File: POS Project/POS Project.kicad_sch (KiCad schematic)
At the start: 15 parts, among them J1 JST_2mm_LiPo, P1 USB_C_Plug_USB2.0, U1 MCP73831-2-OT

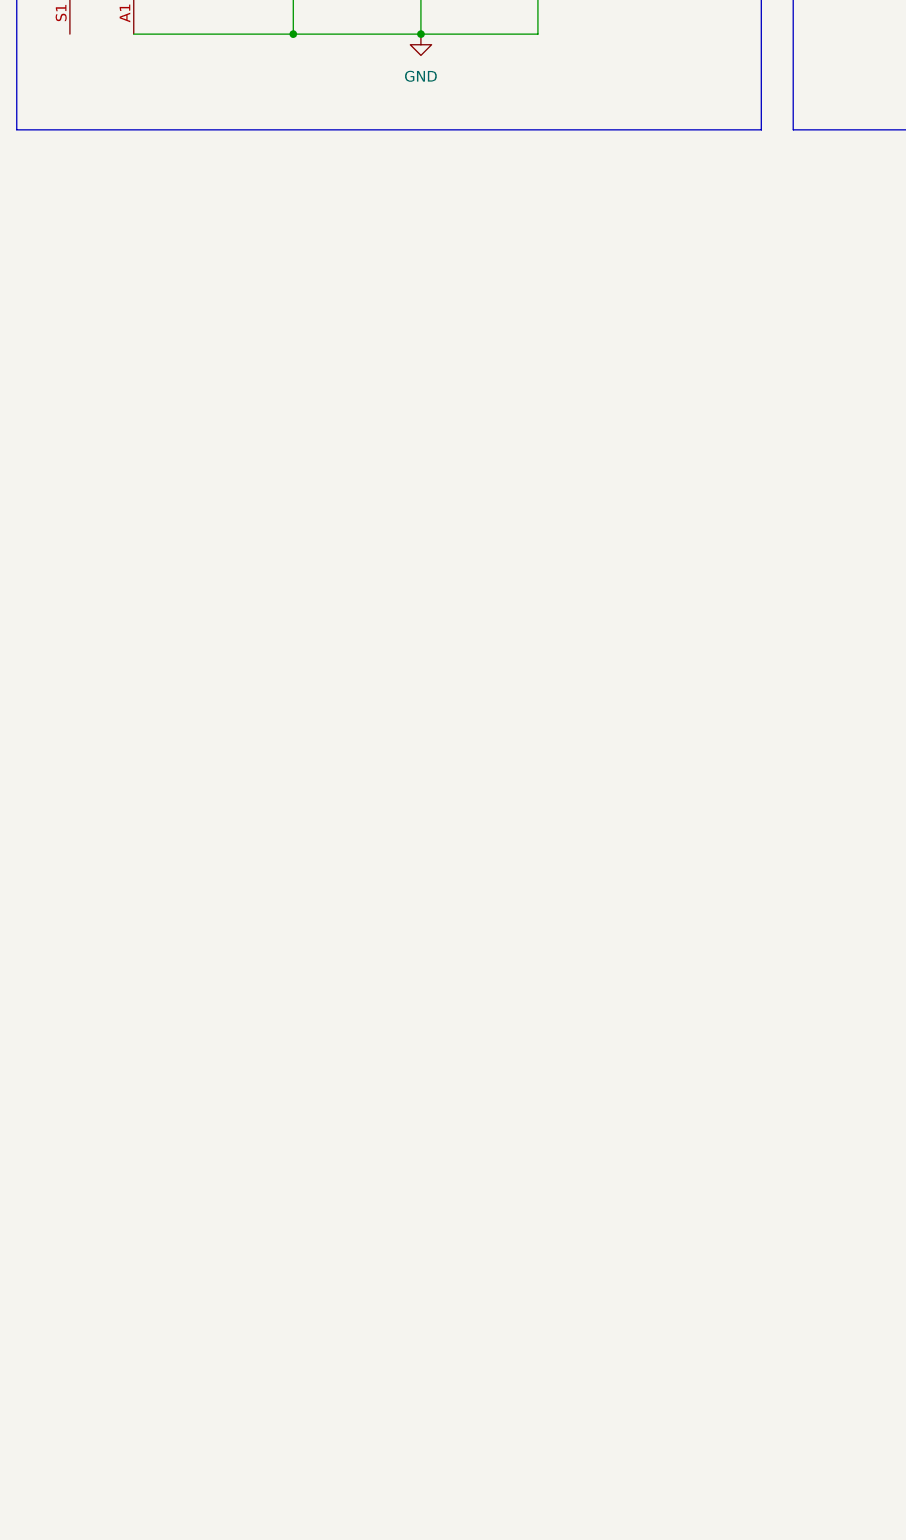
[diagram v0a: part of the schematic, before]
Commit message: modified sim7600x symbol
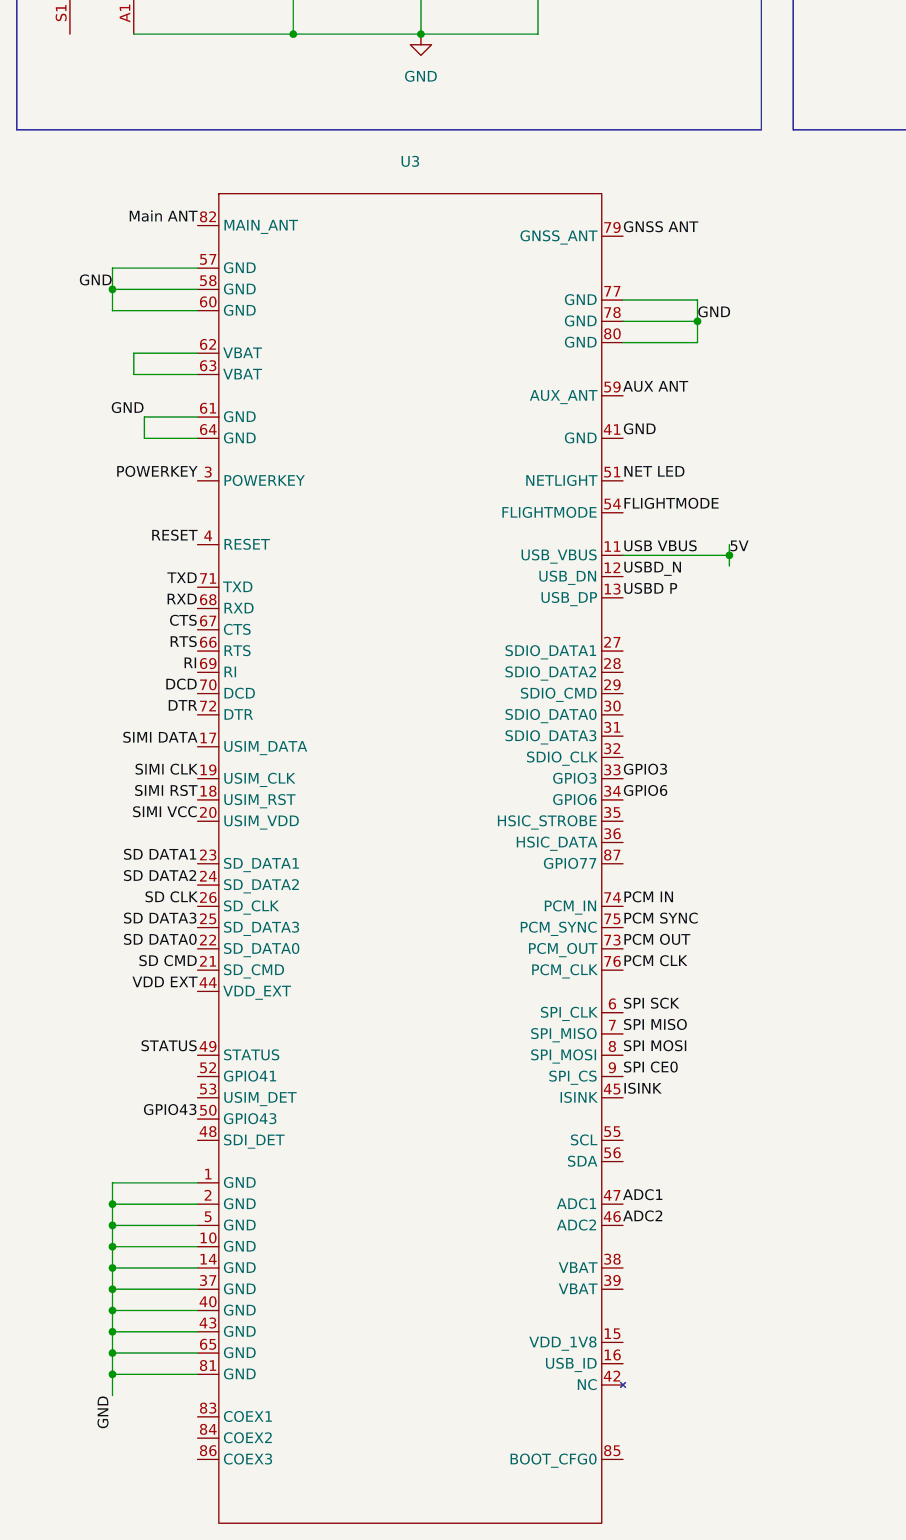
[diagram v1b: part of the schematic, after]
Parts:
- added U3: ~, symbol POSproject:SIM7600Cx
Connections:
- net GND: now also U3.1 (GND), U3.10 (GND), U3.14 (GND), U3.2 (GND), U3.37 (GND), U3.40 (GND), U3.41 (GND), U3.43 (GND), U3.5 (GND), U3.57 (GND), U3.58 (GND), U3.60 (GND), U3.61 (GND), U3.64 (GND), U3.65 (GND), U3.77 (GND), U3.78 (GND), U3.80 (GND), U3.81 (GND)
- new net: U3.62 (VBAT), U3.63 (VBAT)
- new net 5V: U3.11 (USB_VBUS)
- new net ADC1: U3.47 (ADC1)
- new net ADC2: U3.46 (ADC2)
- new net AUX ANT: U3.59 (AUX_ANT)
- new net CTS: U3.67 (CTS)
- new net DCD: U3.70 (DCD)
- new net DTR: U3.72 (DTR)
- new net FLIGHTMODE: U3.54 (FLIGHTMODE)
- new net GNSS ANT: U3.79 (GNSS_ANT)
- new net GPIO3: U3.33 (GPIO3)
- new net GPIO43: U3.50 (GPIO43)
- new net GPIO6: U3.34 (GPIO6)
- new net ISINK: U3.45 (ISINK)
- new net Main ANT: U3.82 (MAIN_ANT)
- new net NET LED: U3.51 (NETLIGHT)
- new net PCM CLK: U3.76 (PCM_CLK)
- new net PCM IN: U3.74 (PCM_IN)
- new net PCM OUT: U3.73 (PCM_OUT)
- new net PCM SYNC: U3.75 (PCM_SYNC)
- new net POWERKEY: U3.3 (POWERKEY)
- new net RESET: U3.4 (RESET)
- new net RI: U3.69 (RI)
- new net RTS: U3.66 (RTS)
- new net RXD: U3.68 (RXD)
- new net SD CLK: U3.26 (SD_CLK)
- new net SD CMD: U3.21 (SD_CMD)
- new net SD DATA0: U3.22 (SD_DATA0)
- new net SD DATA1: U3.23 (SD_DATA1)
- new net SD DATA2: U3.24 (SD_DATA2)
- new net SD DATA3: U3.25 (SD_DATA3)
- new net SIMI CLK: U3.19 (USIM_CLK)
- new net SIMI DATA: U3.17 (USIM_DATA)
- new net SIMI RST: U3.18 (USIM_RST)
- new net SIMI VCC: U3.20 (USIM_VDD)
- new net SPI CE0: U3.9 (SPI_CS)
- new net SPI MISO: U3.7 (SPI_MISO)
- new net SPI MOSI: U3.8 (SPI_MOSI)
- new net SPI SCK: U3.6 (SPI_CLK)
- new net STATUS: U3.49 (STATUS)
- new net TXD: U3.71 (TXD)
- new net USBD P: U3.13 (USB_DP)
- new net USBD_N: U3.12 (USB_DN)
- new net VDD EXT: U3.44 (VDD_EXT)

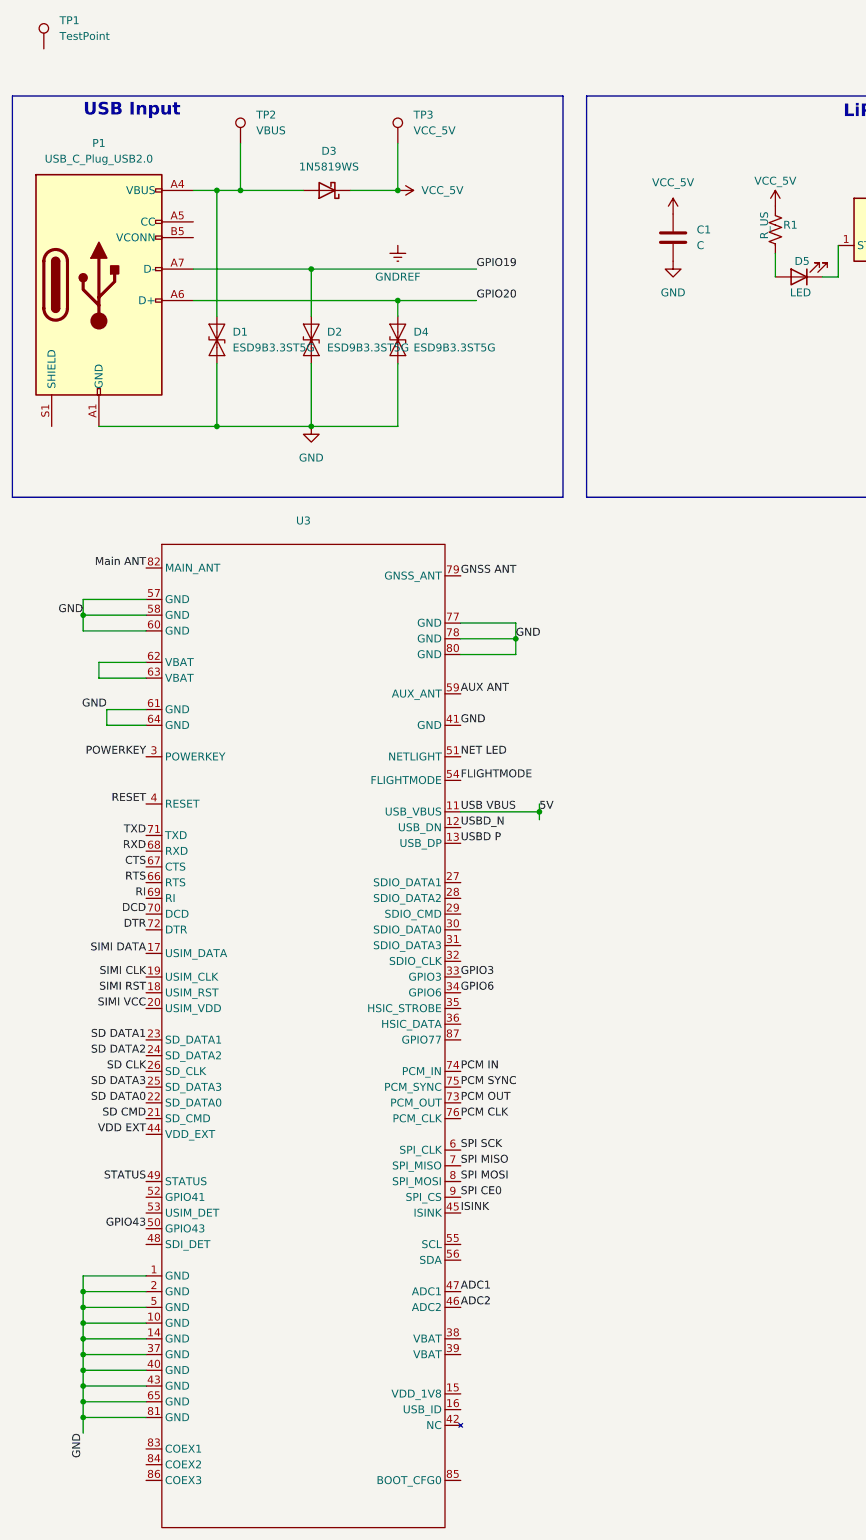
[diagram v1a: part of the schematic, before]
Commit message: updated SIM7600x scematic
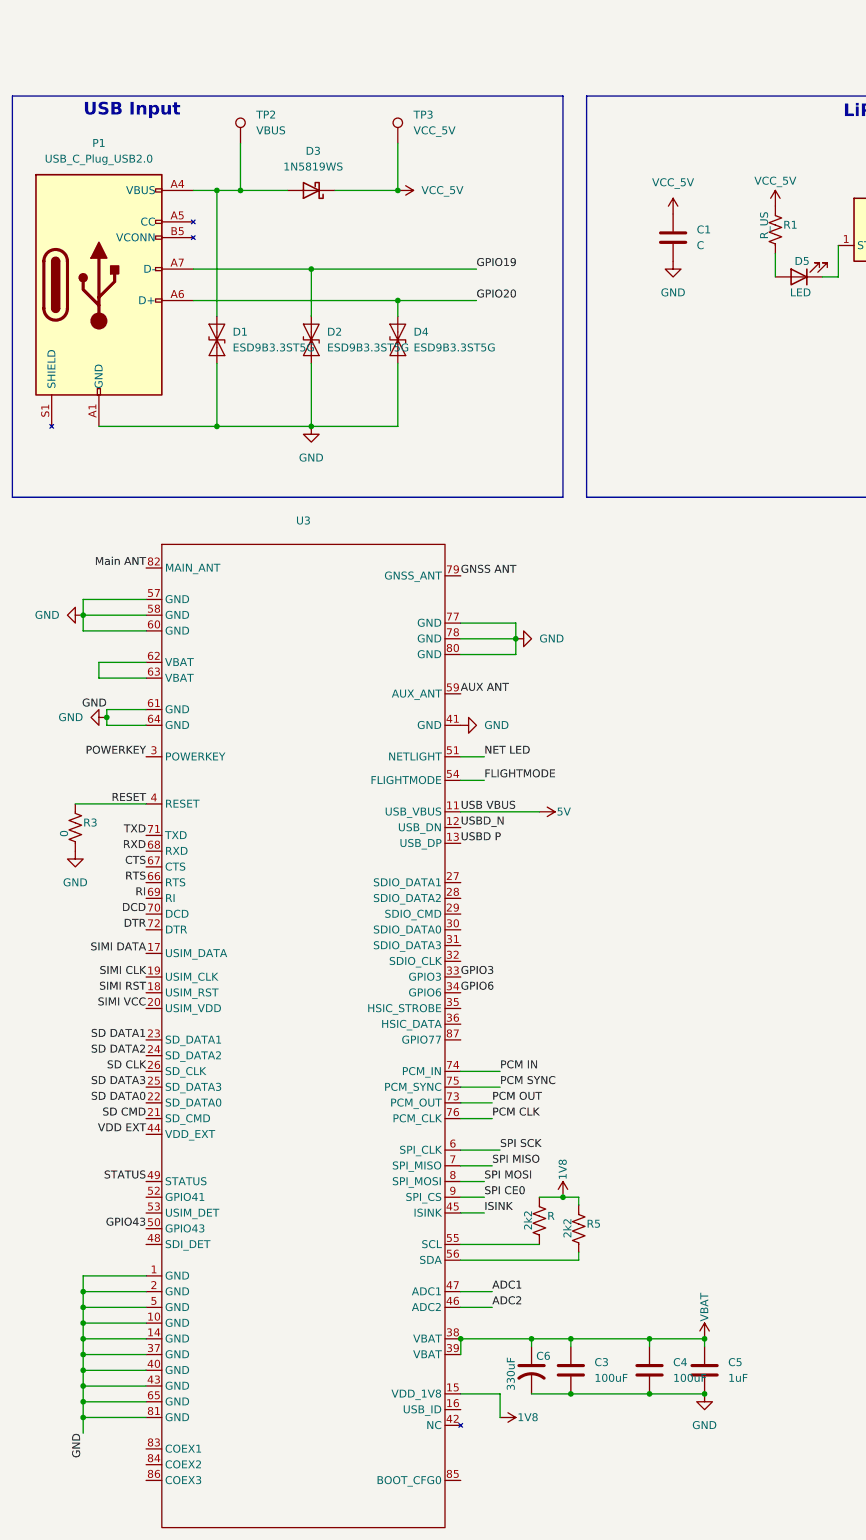
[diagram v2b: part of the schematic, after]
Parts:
- removed TP1: TestPoint, symbol Connector:TestPoint
- added C3, C4: 100uF, symbol Device:C
- added C5: 1uF, symbol Device:C
- added C6: 330uF, symbol Device:C_US
- added R, R5: 2k2, symbol Device:R_US
- added R3: 0, symbol Device:R_US
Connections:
- net GND: now also C3.2, C4.2, C5.2, C6.2, R3.2
- net RESET: now also R3.1
- net 1V8: now reaches U3.15 (VDD_1V8)
- net 1V8: now also R.1, R5.1
- net VBAT: now reaches U3.38 (VBAT)
- net VBAT: now also U3.39 (VBAT), C3.1, C4.1, C5.1, C6.1
- net at U3.55 (SCL): now also R.2
- net at U3.56 (SDA): now also R5.2
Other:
- moved on the sheet: D3

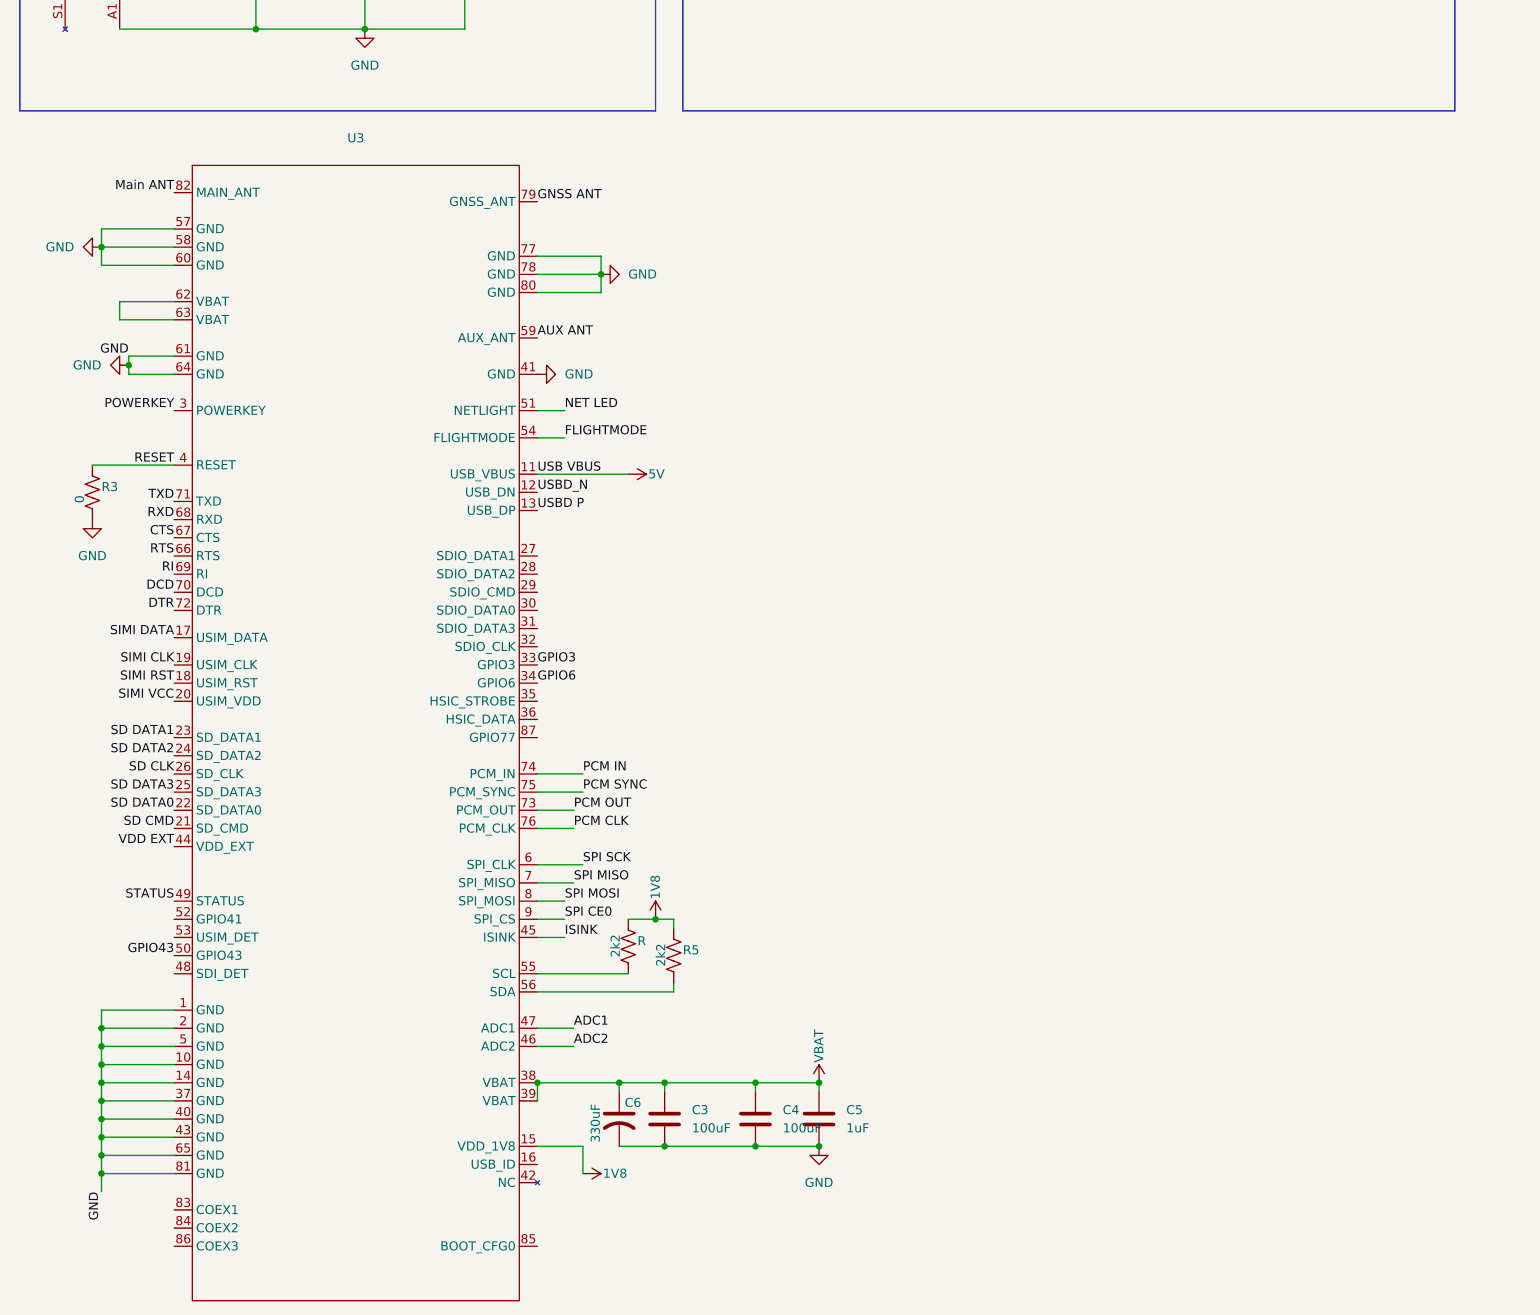
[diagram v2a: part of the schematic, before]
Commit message: added sim card and tvs1 schematic
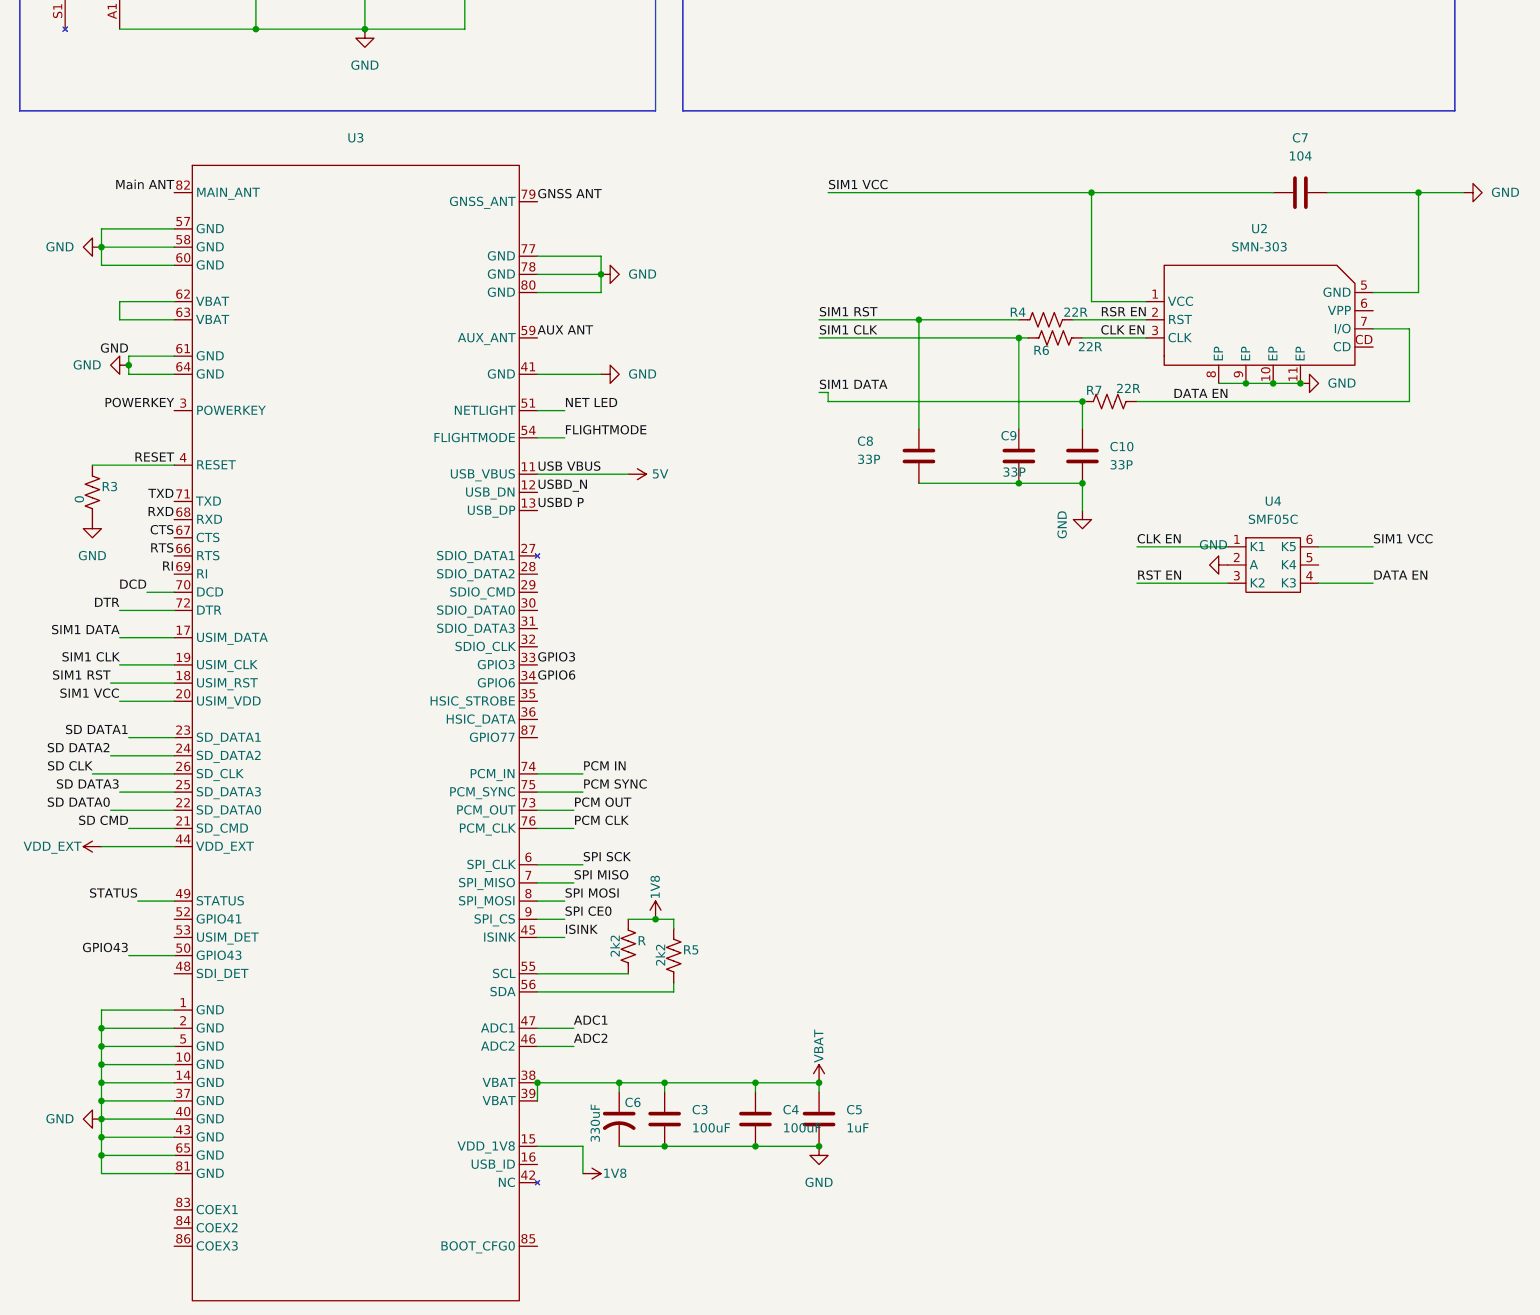
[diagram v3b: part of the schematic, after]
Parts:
- added C10, C8, C9: 33P, symbol Device:C
- added C7: 104, symbol Device:C
- added R4, R6, R7: 22R, symbol Device:R_US
- added U2: SMN-303, symbol POSproject:SIM_Card
- added U4: SMF05C, symbol POSproject:SMF05C
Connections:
- net GND: now also C10.1, C7.2, C8.1, C9.1, U2.10 (EP), U2.11 (EP), U2.5 (GND), U2.8 (EP), U2.9 (EP), U4.2 (A)
- net SIMI CLK renamed SIM1 CLK
- net SIM1 CLK: now also C9.2, R6.1
- net SIMI DATA renamed SIM1 DATA
- net SIM1 DATA: now also C10.2, R7.1
- net SIMI RST renamed SIM1 RST
- net SIM1 RST: now also C8.2, R4.1
- net SIMI VCC renamed SIM1 VCC
- net SIM1 VCC: now also C7.1, U2.1 (VCC), U4.6 (K5)
- net VDD EXT renamed VDD_EXT
- new net CLK EN: R6.2, U2.3 (CLK), U4.1 (K1)
- new net DATA EN: R7.2, U2.7 (I/O), U4.4 (K3)
- new net RSR EN: R4.2, U2.2 (RST)
- new net RST EN: U4.3 (K2)
